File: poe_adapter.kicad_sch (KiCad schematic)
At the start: 24 parts

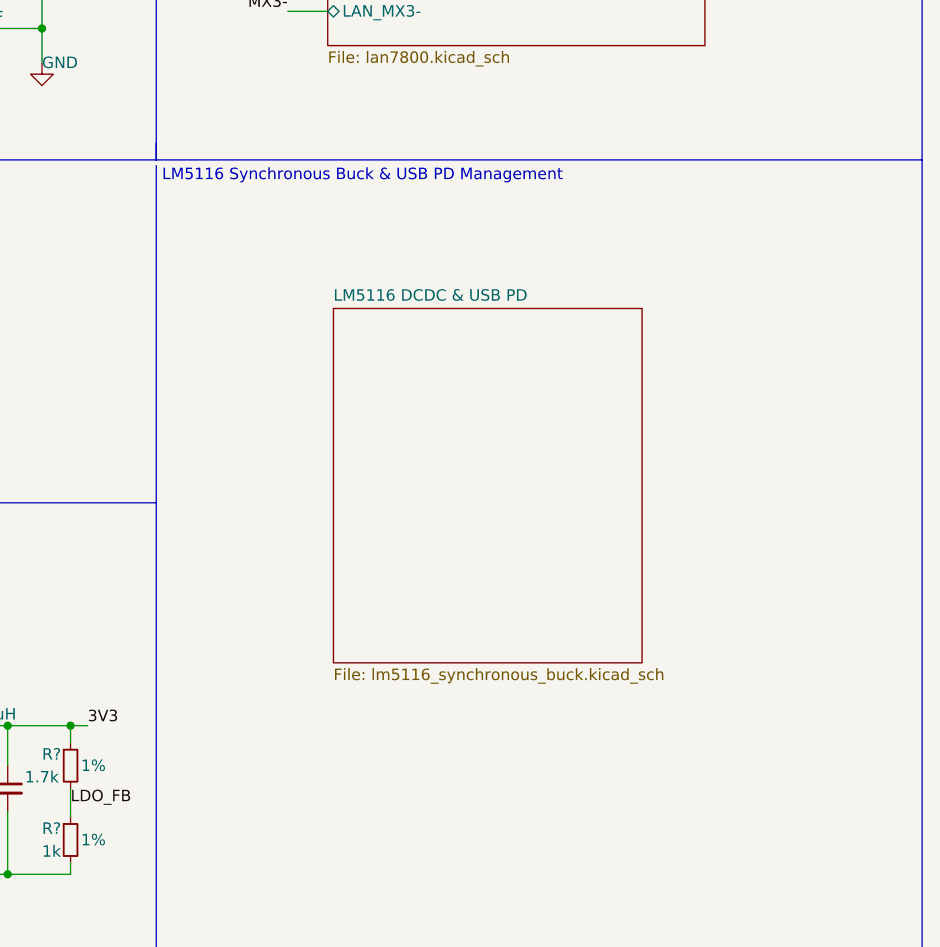
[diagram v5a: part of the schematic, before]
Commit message: finished schema of lm5116 and USB4700
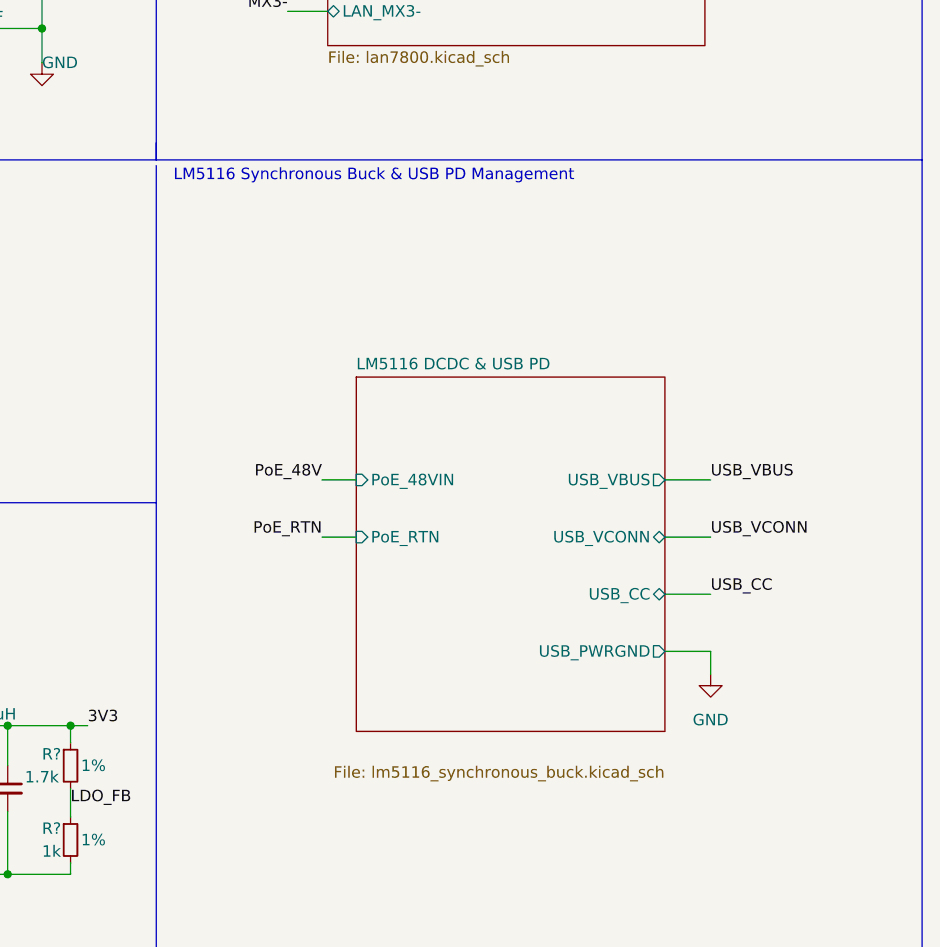
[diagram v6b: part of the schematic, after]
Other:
- sheet LM5116 DCDC & USB PD ports: added PoE_48VIN, PoE_RTN, USB_CC, USB_PWRGND, USB_VBUS, USB_VCONN; removed none

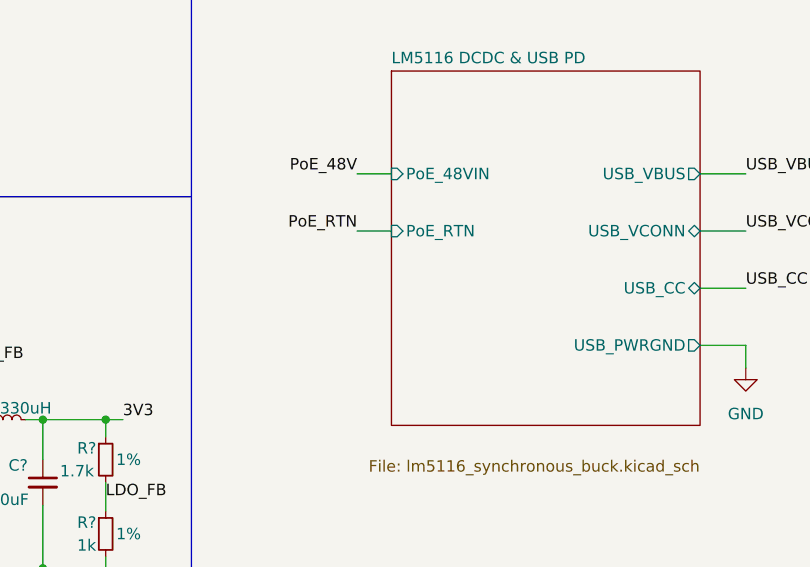
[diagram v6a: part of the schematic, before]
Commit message: added 3v3 for scl & sda pins on stusb4700
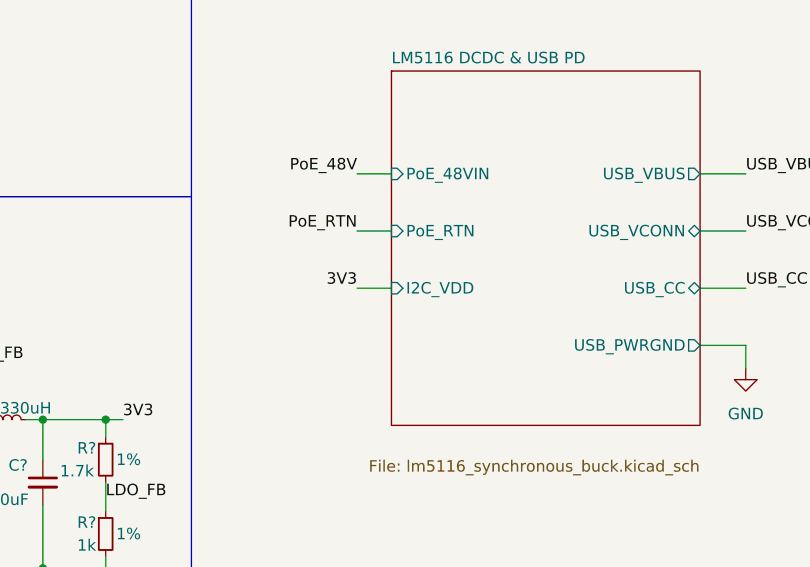
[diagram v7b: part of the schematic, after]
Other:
- sheet LM5116 DCDC & USB PD ports: added I2C_VDD; removed none
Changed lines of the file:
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@@
+    (stroke (width 0) (type default) (color 0 0 0 0))
+  )
+  (wire (pts (xy 185.42 124.46) (xy 189.23 124.46))
     (stroke (width 0) (type default) (color 0 0 0 0))
   )
@@
   (label "RJ45_DB-" (at 67.945 34.29 0)
     (effects (font (size 1.27 1.27)) (justify left bottom))
+  )
+  (label "3V3" (at 185.42 124.46 180)
+    (effects (font (size 1.27 1.27)) (justify right bottom))
   )
   (label "USB_CC" (at 228.6 124.46 0)
@@
       (effects (font (size 1.27 1.27)) (justify left))
     )
+    (pin "I2C_VDD" input (at 189.23 124.46 180)
+      (effects (font (size 1.27 1.27)) (justify left))
+    )
   )
   (sheet (at 107.315 83.185) (size 27.94 19.05) (fields_autoplaced)
@@
       (reference "#PWR?") (unit 1) (value "+3V3") (footprint "")
     )
+    (path "/2ca3a0f2-1db2-49ca-b941-3735f746c2ef/d3c70f33-e011-4fb8-a1bd-f04ec0e34d05"
+      (reference "#PWR?") (unit 1) (value "VSS") (footprint "")
+    )
     (path "/2ca3a0f2-1db2-49ca-b941-3735f746c2ef/d4d76da9-4fb0-49b8-a288-70301089f040"
       (reference "#PWR?") (unit 1) (value "VSS") (footprint "")
@@
       (reference "J?") (unit 1) (value "Conn_01x02") (footprint "TestPoint:TestPoint_2Pads_Pitch2.54mm_Drill0.8mm")
     )
+    (path "/2ca3a0f2-1db2-49ca-b941-3735f746c2ef/cc14e1d4-4f25-4968-a538-fd991eca7ecb"
+      (reference "J?") (unit 1) (value "Conn_01x03_Male") (footprint "")
+    )
     (path "/2ca3a0f2-1db2-49ca-b941-3735f746c2ef/f896b6f2-a4ee-453d-8853-a2e94a7ca9d6"
       (reference "J?") (unit 1) (value "Conn_01x01_Male") (footprint "")
@@
       (reference "R?") (unit 1) (value "16k") (footprint "")
     )
+    (path "/2ca3a0f2-1db2-49ca-b941-3735f746c2ef/1e46cf2c-a297-4ead-9702-981df8e6ac55"
+      (reference "R?") (unit 1) (value "4.7k") (footprint "")
+    )
     (path "/51efc304-0253-4cf9-b8a4-37a603089f63/2d2c2a42-f716-4dfe-81c9-28e3c3dc854b"
       (reference "R?") (unit 1) (value "24.9k") (footprint "")
@@
       (reference "R?") (unit 1) (value "11.5k") (footprint "")
     )
+    (path "/2ca3a0f2-1db2-49ca-b941-3735f746c2ef/da509481-08db-43d1-96ea-01ae676ccfc3"
+      (reference "R?") (unit 1) (value "4.7k") (footprint "")
+    )
     (path "/51efc304-0253-4cf9-b8a4-37a603089f63/dafab510-7158-46c4-a0db-1592c39b22b5"

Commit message: power symbol updated
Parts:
- removed P?: USB_C_Plug, Connector_USB:USB_C_Plug_Molex_105444, symbol Connector:USB_C_Plug
- added J?: USB_C_Receptacle, symbol Connector:USB_C_Receptacle
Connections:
- net Earth_Protective: now also J?.S1 (SHIELD)
- net GND: now also J?.A1 (GND), J?.A12 (GND), J?.B1 (GND), J?.B12 (GND)
- net USB_CC: now also J?.A5 (CC1)
- net USB_SBU1: now also J?.A8 (SBU1)
- net USB_SBU2: now also J?.B8 (SBU2)
- net USB_TX1+: now also J?.A2 (TX1+)
- net USB_TX1-: now also J?.A3 (TX1-)
- net USB_VBUS: now also J?.A4 (VBUS), J?.A9 (VBUS), J?.B4 (VBUS), J?.B9 (VBUS)
- net USB_VCONN: now also J?.B5 (CC2)
- net at C?.1: now also J?.B11 (RX1+)
- net at R?.1: now also J?.A6 (D+)
- net at C?.1: now also J?.B10 (RX1-)
- net at R?.1: now also J?.A7 (D-)
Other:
- note added: "*Net labels only connect on the same sheet. *Global labels connect globally (across all sheets). *Hierarchical labels connect within sheet borders and to the hierarchical sheet boxes, where the labels can be imported from the underlying schematic."
- note added: "Earth ground, ESD protection Connect to all shield"
- note added: "Global Ground, Defined Zero directly connected to silicons voltage 0"
- note added: "Global Powers"
- note added: "Power Ground directly connected to GND voltage 0"
- note added: "VSS directly connected to silicons and GND voltage 0"
